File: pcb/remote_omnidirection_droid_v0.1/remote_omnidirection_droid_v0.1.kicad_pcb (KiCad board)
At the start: 2 copper layers, 120 x 103.9 mm, 53 parts, among them J1 USB_C_Receptacle_USB2.0, J2 Conn_01x04, J3 BATT_CONNECT, J4 Conn_01x04, J5 Conn_01x04, M1 Motor_DC_ALT, M2 Motor_DC_ALT, M3 Motor_DC_ALT, Q1 BC846BS, SW1 SW_SPST, SW2 SW_SPST, SW3 SW_SPDT, U1 AZ1117-3.3, U2 AZ1117-5.0, U3 USBLC6-2SC6, U4 ESP32-S3-WROOM-2-N32R8V

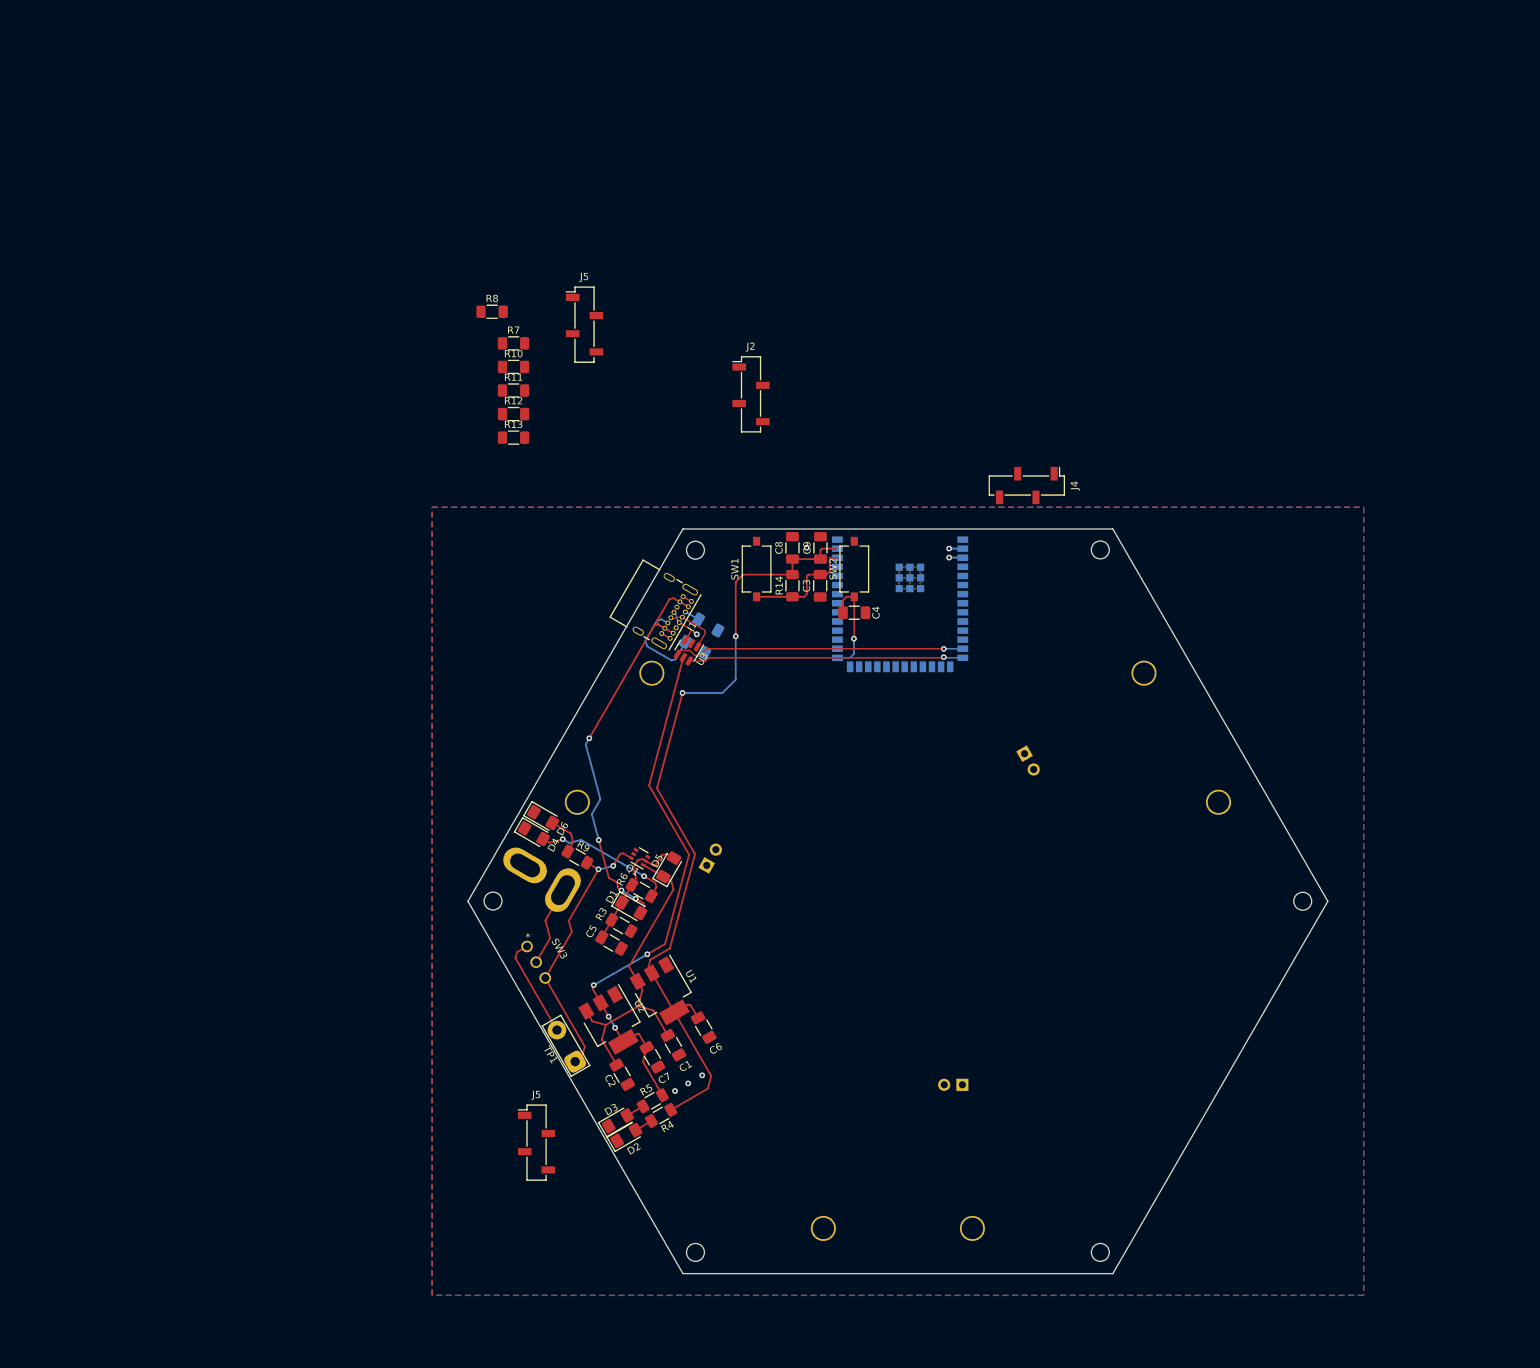
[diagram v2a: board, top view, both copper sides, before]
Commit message: added BNO055
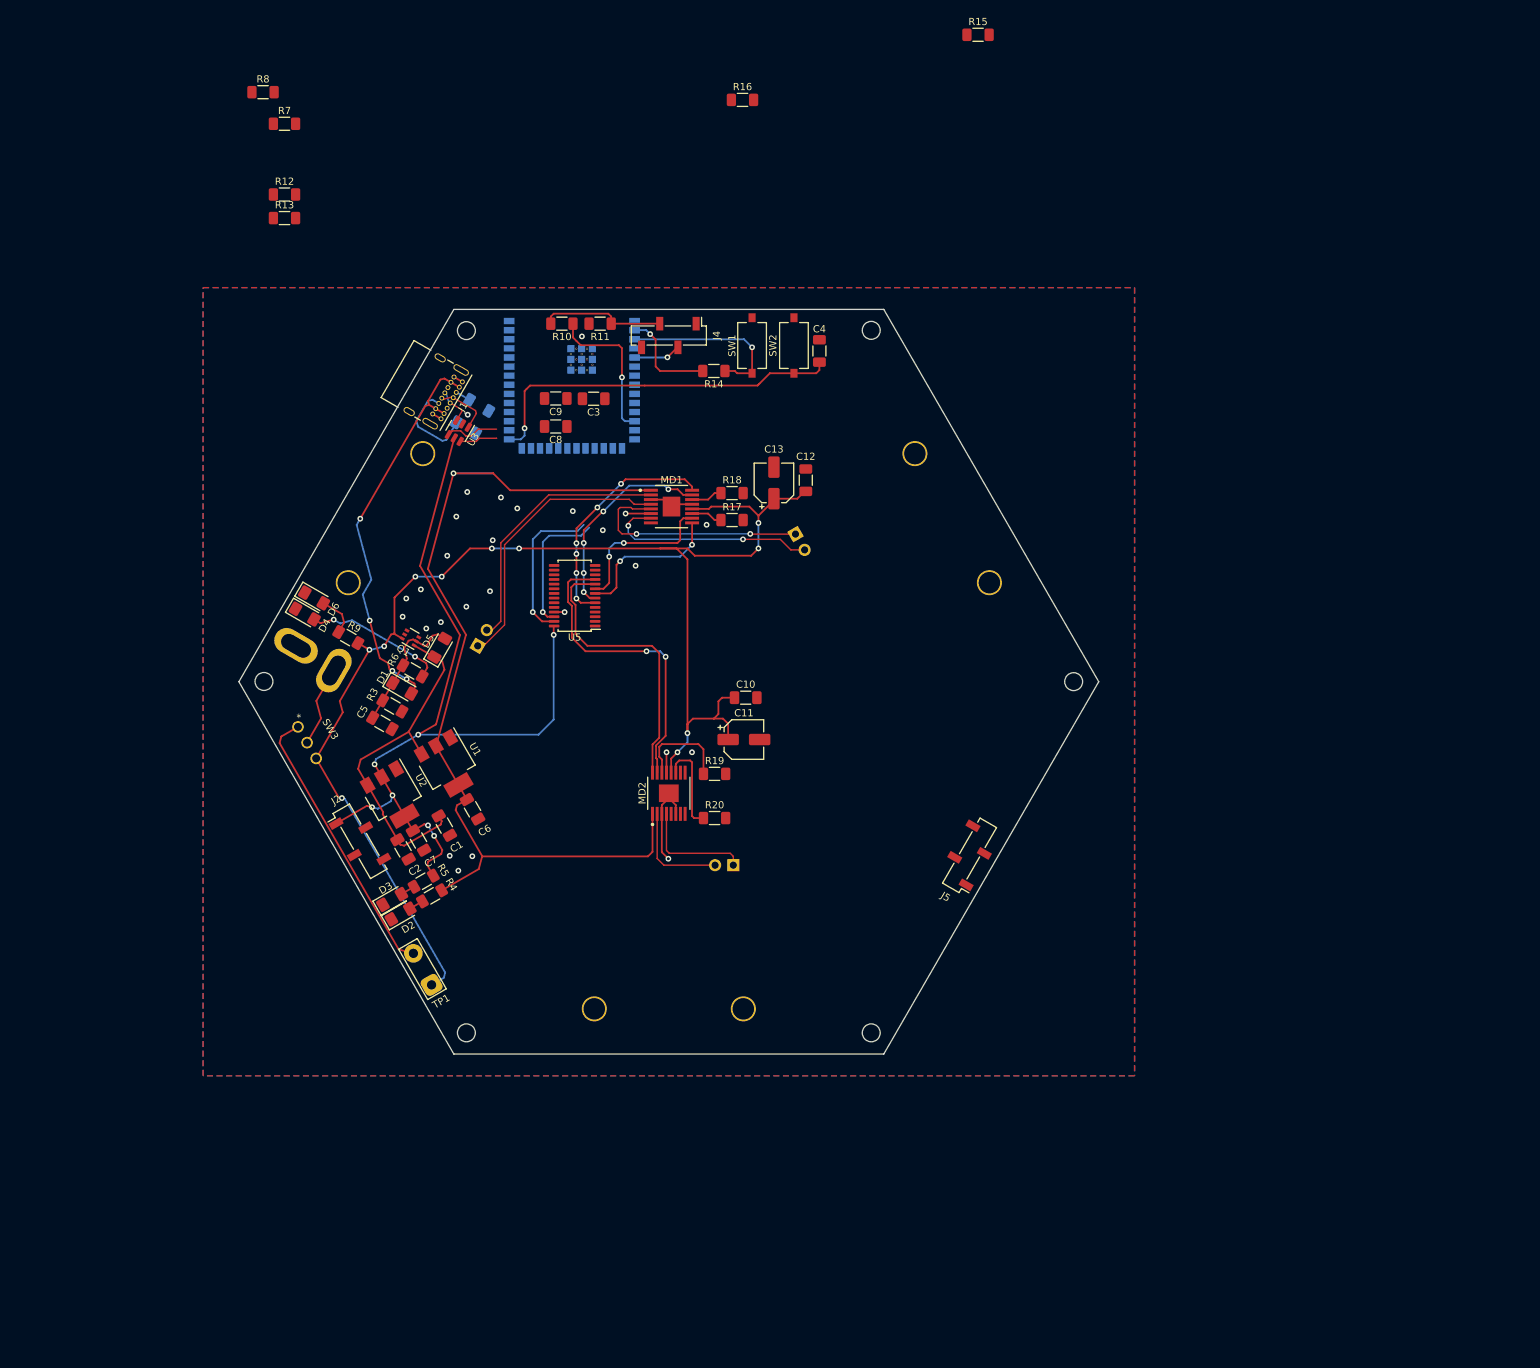
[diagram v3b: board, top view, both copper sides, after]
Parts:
- removed the J5 at (95.7, 166.6)
- added C10: 100n, Capacitor_SMD:C_1206_3216Metric_Pad1.33x1.80mm_HandSolder, F.Cu at (124.9, 104.5)
- added C11: 10u, Capacitor_SMD:CP_Elec_5x5.3, F.Cu at (124.6, 110.3)
- added C12: 100n, Capacitor_SMD:C_1206_3216Metric_Pad1.33x1.80mm_HandSolder, F.Cu at (133.3, 74.1)
- added C13: 10u, Capacitor_SMD:CP_Elec_5x5.3, F.Cu at (128.8, 74.5)
- added MD1: DRV8411, Drone_Footprints:PWP0016C-IPC_A, F.Cu at (114.5, 77.8)
- added MD2: DRV8411, Drone_Footprints:PWP0016C-IPC_A, F.Cu at (114.1, 117.8)
- added R15: 5.1k, Resistor_SMD:R_1206_3216Metric_Pad1.30x1.75mm_HandSolder, F.Cu at (157.3, 12.0)
- added R16: 5.1k, Resistor_SMD:R_1206_3216Metric_Pad1.30x1.75mm_HandSolder, F.Cu at (124.4, 21.1)
- added R17: 22k, Resistor_SMD:R_1206_3216Metric_Pad1.30x1.75mm_HandSolder, F.Cu at (123.0, 79.7)
- added R18: 22k, Resistor_SMD:R_1206_3216Metric_Pad1.30x1.75mm_HandSolder, F.Cu at (123.0, 75.9)
- added R19: 22k, Resistor_SMD:R_1206_3216Metric_Pad1.30x1.75mm_HandSolder, F.Cu at (120.5, 115.1)
- added R20: 22k, Resistor_SMD:R_1206_3216Metric_Pad1.30x1.75mm_HandSolder, F.Cu at (120.5, 121.3)
- added U5: PCA9685PW, Package_SO:TSSOP-28_4.4x9.7mm_P0.65mm, F.Cu at (101.0, 90.3)
- moved J5 91.5 mm to (156.1, 126.5), turned to 150 degrees
- moved J2 82.9 mm to (71.0, 124.5), turned to 30 degrees
- moved U4 55.0 mm to (100.6, 57.2)
- moved J4 54.2 mm to (114.1, 53.9)
- moved C7 44.5 mm to (79.2, 124.4)
- moved C6 44.4 mm to (86.7, 120.1)
- moved J1 44.3 mm to (85.3, 60.4)
- moved R3 44.3 mm to (75.6, 105.6)
- moved R9 44.3 mm to (69.4, 96.1)
- moved R2 44.3 mm to (87.7, 63.7)
- moved J3 44.3 mm to (64.5, 99.1)
- moved R13 44.3 mm to (60.5, 37.6)
- moved R5 44.3 mm to (79.9, 130.1)
- moved H5 44.3 mm to (142.4, 151.3)
- moved H1 44.3 mm to (57.6, 102.2)
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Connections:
- M1 pad 1: unconnected-(M1-+-Pad1) -> /MOTOR1+
- M1 pad 2: unconnected-(M1---Pad2) -> /MOTOR1-
- M2 pad 1: unconnected-(M2-+-Pad1) -> /MOTOR2+
- M2 pad 2: unconnected-(M2---Pad2) -> /MOTOR2-
- M3 pad 1: unconnected-(M3-+-Pad1) -> /MOTOR3+
- M3 pad 2: unconnected-(M3---Pad2) -> /MOTOR3-
- U4 pad 12: unconnected-(U4-IO8-Pad12) -> /ECHO2
- U4 pad 17: unconnected-(U4-IO9-Pad17) -> /ECHO3
- U4 pad 34: unconnected-(U4-IO41-Pad34) -> /SCL
- U4 pad 35: unconnected-(U4-IO42-Pad35) -> /SDA
- U4 pad 4: unconnected-(U4-IO4-Pad4) -> /TRIG1
- U4 pad 5: unconnected-(U4-IO5-Pad5) -> /TRIG2
- U4 pad 6: unconnected-(U4-IO6-Pad6) -> /TRIG3
- U4 pad 7: unconnected-(U4-IO7-Pad7) -> /ECHO1
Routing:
- net +BATT: track 38.7 -> 195.1 mm, vias 2 -> 11
- net /PWM6: track 0.00 -> 42.9 mm, vias 0 -> 2
- net +5V: track 75.2 -> 117.1 mm, vias 4 -> 7
- net /PWM5: track 0.00 -> 40.1 mm
- net /MOTOR1+: track 0.00 -> 39.5 mm
- net /BOOT: track 14.0 -> 52.1 mm
- net /MOTOR1-: track 0.00 -> 37.1 mm
- net /D+: track 38.4 -> 5.26 mm, vias 1 -> 0
- net /D-: track 40.7 -> 7.62 mm, vias 1 -> 0
- net /MOTOR2+: track 0.00 -> 32.6 mm, vias 0 -> 2
- net /PWM1: track 0.00 -> 32.5 mm, vias 0 -> 6
- net /MOTOR2-: track 0.00 -> 30.4 mm, vias 0 -> 2
- net +3V3: track 114.0 -> 144.2 mm, vias 3 -> 2
- net /PWM2: track 0.00 -> 28.8 mm, vias 0 -> 5
- net GND: track 2.70 -> 29.4 mm, vias 5 -> 27
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
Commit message: board "complete"
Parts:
- added C14: 22u, Capacitor_SMD:C_1206_3216Metric_Pad1.33x1.80mm_HandSolder, F.Cu at (112.2, 113.9)
- added C15: 22u, Capacitor_SMD:C_1206_3216Metric_Pad1.33x1.80mm_HandSolder, F.Cu at (106.2, 103.4)
- added C16: 0.1u, Capacitor_SMD:C_1206_3216Metric_Pad1.33x1.80mm_HandSolder, F.Cu at (97.6, 102.4)
- added C17: 0.1u, Capacitor_SMD:C_1206_3216Metric_Pad1.33x1.80mm_HandSolder, F.Cu at (99.1, 105.1)
- added C18: 10u, Capacitor_SMD:C_1206_3216Metric_Pad1.33x1.80mm_HandSolder, F.Cu at (90.9, 103.0)
- added R21: 10k, Resistor_SMD:R_1206_3216Metric_Pad1.30x1.75mm_HandSolder, F.Cu at (107.1, 119.5)
- added R22: 10k, Resistor_SMD:R_1206_3216Metric_Pad1.30x1.75mm_HandSolder, F.Cu at (108.9, 122.7)
- added R23: 200k, Resistor_SMD:R_1206_3216Metric_Pad1.30x1.75mm_HandSolder, F.Cu at (87.9, 97.8)
- added U6: BNO055, Package_LGA:LGA-28_5.2x3.8mm_P0.5mm, F.Cu at (102.9, 112.3)
- added U7: PCA9306D, Package_SO:SO-8_3.9x4.9mm_P1.27mm, F.Cu at (94.4, 97.9)
- added Y1: 32.768kHz, Crystal:Crystal_SMD_Abracon_ABS25-4Pin_8.0x3.8mm, F.Cu at (109.3, 108.6)
- J1: footprint Connector_USB:USB_C_Receptacle_GCT_USB4085 -> Connector_USB:USB_C_Receptacle_GCT_USB4105-xx-A_16P_TopMnt_Horizontal
- R15, R16: value 5.1k -> 10k
- moved R12 137.4 mm to (114.1, 160.8), turned to -90 degrees
- moved R13 133.0 mm to (110.5, 160.8), turned to 90 degrees
- moved R15 99.1 mm to (96.2, 90.1), turned to 30 degrees
- moved R16 76.9 mm to (98.1, 93.3), turned to 30 degrees
- moved R8 72.7 mm to (58.0, 92.7), turned to -30 degrees
- moved H4 71.0 mm to (131.2, 161.2), turned to -60 degrees
- moved R7 70.7 mm to (56.7, 95.0), turned to -30 degrees
- moved H5 68.5 mm to (74.6, 161.3), turned to -60 degrees
- moved J5 63.3 mm to (102.9, 160.8), turned to 90 degrees
- moved H3 61.5 mm to (159.5, 112.2), turned to -60 degrees
- moved H6 55.5 mm to (46.4, 112.3), turned to -60 degrees
- moved C4 54.5 mm to (153.4, 107.4), turned to 30 degrees
- moved SW2 52.8 mm to (152.3, 104.0), turned to -150 degrees
- moved SW1 49.6 mm to (149.4, 98.9), turned to -150 degrees
- moved TP1 49.5 mm to (48.2, 107.5), turned to 60 degrees
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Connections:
- R1 pad 1: GND -> /CC1
- R1 pad 2: /CC2 -> GND
- R15 pad 2: /SCL -> /SCL_5V
- R16 pad 2: /SDA -> /SDA_5V
- R2 pad 1: GND -> /CC2
- R2 pad 2: /CC1 -> GND
- U5 pad 26: /SCL -> /SCL_5V
- U5 pad 27: /SDA -> /SDA_5V
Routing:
- net +5V: track 117.1 -> 249.8 mm, vias 7 -> 17
- net +3V3: track 144.2 -> 267.2 mm, vias 2 -> 7
- net /TRIG3: track 0.00 -> 107.0 mm, vias 0 -> 1
- net /ECHO1: track 0.00 -> 105.3 mm, vias 0 -> 9
- net /TRIG1: track 0.00 -> 97.1 mm, vias 0 -> 9
- net /ECHO3: track 0.00 -> 84.9 mm, vias 0 -> 5
- net /SDA: track 21.6 -> 101.4 mm, vias 1 -> 4
- net /SCL: track 18.9 -> 95.5 mm, vias 1 -> 5
- net /EN: track 24.4 -> 51.6 mm, vias 1 -> 3
- net /SCL_5V: track 0.00 -> 24.0 mm, vias 0 -> 2
- net /D-: track 7.62 -> 26.1 mm, vias 0 -> 1
- net /D+: track 5.26 -> 23.5 mm, vias 0 -> 1
- net /SDA_5V: track 0.00 -> 17.0 mm
- net Net-(U7-EN): track 0.00 -> 15.8 mm, vias 0 -> 2
- net Net-(U6-CAP): track 0.00 -> 12.8 mm
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
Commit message: near finalized v0.1
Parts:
- added BZ1: Buzzer, Buzzer_Beeper:Buzzer_12x9.5RM7.6, F.Cu at (159.7, 92.0)
- added D7: 1N4148W, Diode_SMD:D_SOD-123, F.Cu at (148.9, 92.5)
- added IO15: TestPoint, TestPoint:TestPoint_THTPad_D2.5mm_Drill1.2mm, F.Cu at (145.6, 51.8)
- added IO16: TestPoint, TestPoint:TestPoint_THTPad_D2.5mm_Drill1.2mm, F.Cu at (143.2, 47.7)
- added IO17: TestPoint, TestPoint:TestPoint_THTPad_D2.5mm_Drill1.2mm, F.Cu at (149.7, 49.5)
- added IO18: TestPoint, TestPoint:TestPoint_THTPad_D2.5mm_Drill1.2mm, F.Cu at (147.3, 45.4)
- added J6: Conn_01x03, Connector_PinHeader_2.54mm:PinHeader_1x03_P2.54mm_Vertical, F.Cu at (91.9, 65.1)
- added Q2: 2N2219, Package_TO_SOT_THT:TO-92L_Inline, F.Cu at (149.3, 89.4)
- added R24: 180, Resistor_SMD:R_1206_3216Metric_Pad1.30x1.75mm_HandSolder, F.Cu at (148.8, 84.1)
- H1, H2, H3, H4, H5, H6: footprint MountingHole:MountingHole_2.5mm -> MountingHole:MountingHole_2.7mm_M2.5
- moved H4 129.1 mm to (87.3, 39.8), turned to 0 degrees
- moved H5 121.2 mm to (171.3, 88.2), turned to 0 degrees
- moved H6 121.1 mm to (143.3, 39.8), turned to 0 degrees
- moved H1 100.5 mm to (143.3, 136.7), turned to 0 degrees
- moved H3 76.2 mm to (87.3, 136.7), turned to 0 degrees
- moved H2 76.1 mm to (59.3, 88.2), turned to 0 degrees
- moved R12 75.6 mm to (162.8, 103.0), turned to -30 degrees
- moved R13 74.5 mm to (161.0, 106.1), turned to 150 degrees
- moved J5 72.6 mm to (157.2, 112.6), turned to 150 degrees
- moved C4 67.4 mm to (136.3, 42.2), turned to 90 degrees
- moved SW2 65.5 mm to (132.7, 41.5), turned to -90 degrees
- moved SW1 61.7 mm to (126.9, 41.5), turned to -90 degrees
- moved M2 60.4 mm to (145.8, 70.8), turned to -60 degrees
- moved J4 56.4 mm to (115.3, 40.1), turned to -90 degrees
- moved R14 55.6 mm to (121.5, 45.0), turned to 180 degrees
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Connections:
- MD1 pad 8: /nFAULT -> unconnected-(MD1-nFAULT-Pad8)
- MD2 pad 8: /nFAULT1 -> unconnected-(MD2-nFAULT-Pad8)
- U4 pad 10: unconnected-(U4-IO17-Pad10) -> /IO17
- U4 pad 11: unconnected-(U4-IO18-Pad11) -> /IO18
- U4 pad 18: unconnected-(U4-IO10-Pad18) -> /BUZZER
- U4 pad 39: unconnected-(U4-IO1-Pad39) -> /NeoPixel
- U4 pad 8: unconnected-(U4-IO15-Pad8) -> /IO15
- U4 pad 9: unconnected-(U4-IO16-Pad9) -> /IO16
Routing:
- net /BUZZER: track 0.00 -> 75.4 mm, vias 0 -> 1
- net +5V: track 249.8 -> 312.0 mm
- net /IO17: track 0.00 -> 44.9 mm, vias 0 -> 3
- net /IO18: track 0.00 -> 40.2 mm, vias 0 -> 4
- net /IO15: track 0.00 -> 37.2 mm, vias 0 -> 2
- net /IO16: track 0.00 -> 34.3 mm, vias 0 -> 3
- net /NeoPixel: track 0.00 -> 26.6 mm
- net Net-(BZ1-+): track 0.00 -> 21.7 mm
- net Net-(Q2-B): track 0.00 -> 8.66 mm
- net GND: track 37.4 -> 39.7 mm, vias 49 -> 53
- net +3V3: track 267.2 -> 269.3 mm
- net Net-(SW3-A): track 39.3 -> 38.4 mm
- net Net-(J3-Pin_1): track 11.3 -> 12.2 mm
- net /NESD_D+: track 7.48 -> 8.10 mm
- net +BATT: track 206.1 -> 206.3 mm, vias 13 -> 12
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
